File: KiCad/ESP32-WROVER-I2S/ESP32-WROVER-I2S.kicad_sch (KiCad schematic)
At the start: 31 parts, among them J1 Ext_con, J2 Audio_Con, J3 USB_C_Receptacle_USB2.0_16P, Q1 BSS138, Q2 BSS138, SW1 FLASH, SW2 RESET, U1 ESP32-WROVER, U2 AMS1117-3.3, U3 CH340K

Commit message: ガーバー出力
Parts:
- removed C7: 1u, Capacitor_SMD:C_0603_1608Metric_Pad1.08x0.95mm_HandSolder, symbol Device:C_Small
- removed C8: 0.1u, Capacitor_SMD:C_0603_1608Metric_Pad1.08x0.95mm_HandSolder, symbol Device:C_Small
- removed J3: USB_C_Receptacle_USB2.0_16P, Connector_USB:USB_C_Receptacle_XKB_U262-16XN-4BVC11, symbol Connector:USB_C_Receptacle_USB2.0_16P
- removed Q1, Q2: BSS138, Package_TO_SOT_SMD:SOT-23, symbol Transistor_FET:BSS138
- removed R5, R6: 5.1k, Resistor_SMD:R_0603_1608Metric_Pad0.98x0.95mm_HandSolder, symbol Device:R_Small_US
- removed SW1: FLASH, Button_Switch_SMD:SW_Push_SPST_NO_Alps_SKRK, symbol Switch:SW_Push
- removed SW2: RESET, Button_Switch_SMD:SW_Push_SPST_NO_Alps_SKRK, symbol Switch:SW_Push
- removed U3: CH340K, Package_SO:SSOP-10-1EP_3.9x4.9mm_P1mm_EP2.1x3.3mm, symbol Interface_USB:CH340K
- added D3: D_Schottky, Diode_SMD:D_SOD-123, symbol Device:D_Schottky
- added J3: Power_Con, Connector_JST:JST_XH_B2B-XH-A_1x02_P2.50mm_Vertical, symbol Connector_Generic:Conn_01x02
- added J4: Downloader, Connector_PinSocket_2.54mm:PinSocket_1x06_P2.54mm_Vertical, symbol Connector_Generic:Conn_01x06
- J2: footprint Connector_PinHeader_2.54mm:PinHeader_1x03_P2.54mm_Vertical -> Connector_JST:JST_XH_B3B-XH-A_1x03_P2.50mm_Vertical
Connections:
- net +3.3V: now also D3.1 (K), J4.1 (Pin_1); no longer C2.1, U2.2 (VO)
- net EN: now also J4.4 (Pin_4)
- net GND: now also J3.2 (Pin_2), J4.6 (Pin_6)
- net GPIO0: now also J4.5 (Pin_5)
- net RxD0: now also J4.3 (Pin_3)
- net TxD0: now also J4.2 (Pin_2)
- net at F1.1: now also J3.1 (Pin_1)
- new net: C2.1, D3.2 (A), U2.2 (VO)
- no-connect marks 16 -> 13
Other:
- note added: "+3.3V"
- note added: "EN"
- note added: "GND"
- note added: "GPIO0"
- note added: "RxD"
- note added: "TxD"
- moved on the sheet: C1, C2, D1, F1, H1, H2, H3, H4, J1, R1, U2

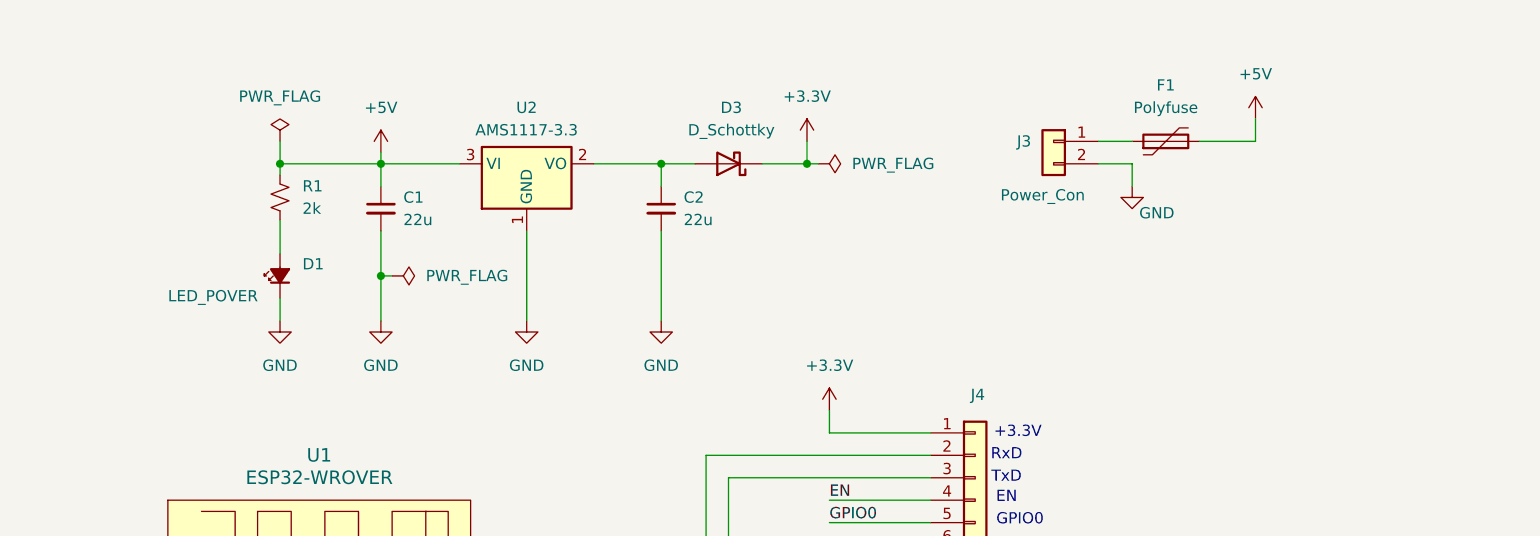
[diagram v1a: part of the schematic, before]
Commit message: 5v/3.3v切り替えジャンパ追加、電源LED変更、REV1.1ガーバー出力
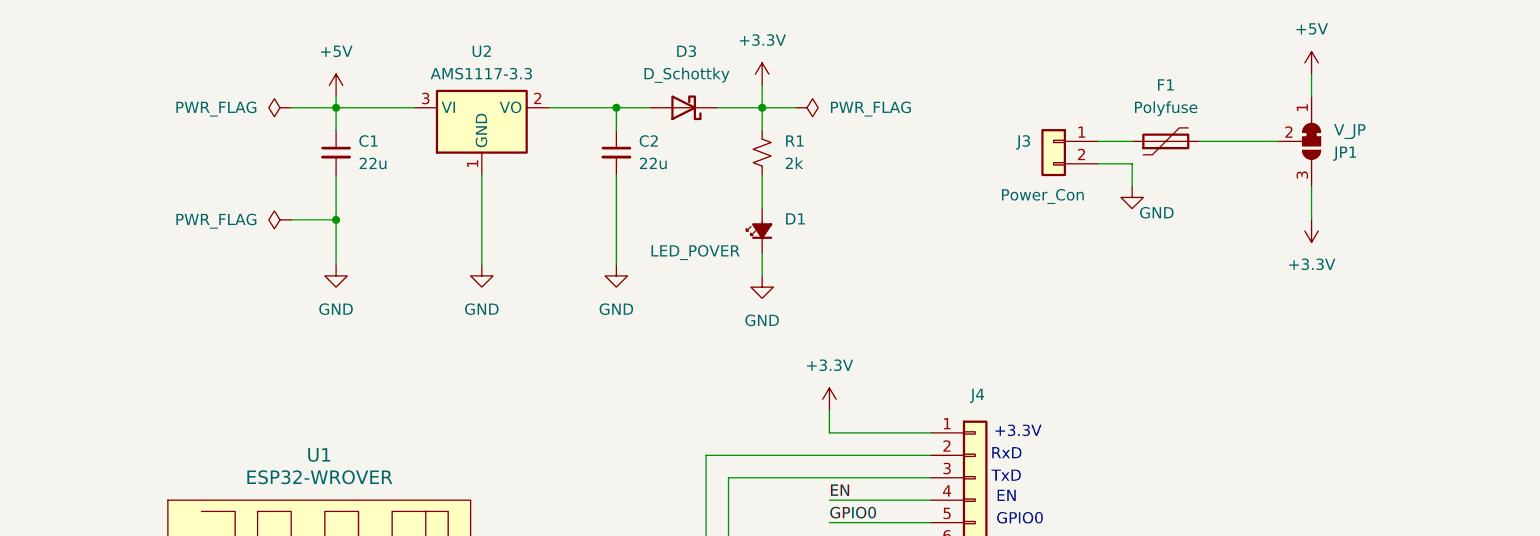
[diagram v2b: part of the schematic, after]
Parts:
- added JP1: V_JP, Jumper:SolderJumper-3_P1.3mm_Bridged12_Pad1.0x1.5mm_NumberLabels, symbol Jumper:SolderJumper_3_Bridged12
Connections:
- net +3.3V: now also R1.1, JP1.3 (B)
- net +5V: now also JP1.1 (A); no longer F1.2, R1.1
- new net: F1.2, JP1.2 (C)
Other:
- moved on the sheet: C1, C2, D1, D3, R1, U2
